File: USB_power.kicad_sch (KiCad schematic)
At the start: 29 parts, among them J14 USB_C_Receptacle_PowerOnly_6P, J16 Conn_01x04, Q3 DMP3013SFV, Q5 DMP3013SFV, U5 CYPD3177-24LQ

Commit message: some changes
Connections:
- net +3.3V is gone; now on net +3.3V_PD: R11.2, R14.2, R16.2, R18.2, R8.2
- net +3.3V_PD: now reaches C52.2, C53.2, C54.2, U5.23 (VDDD)

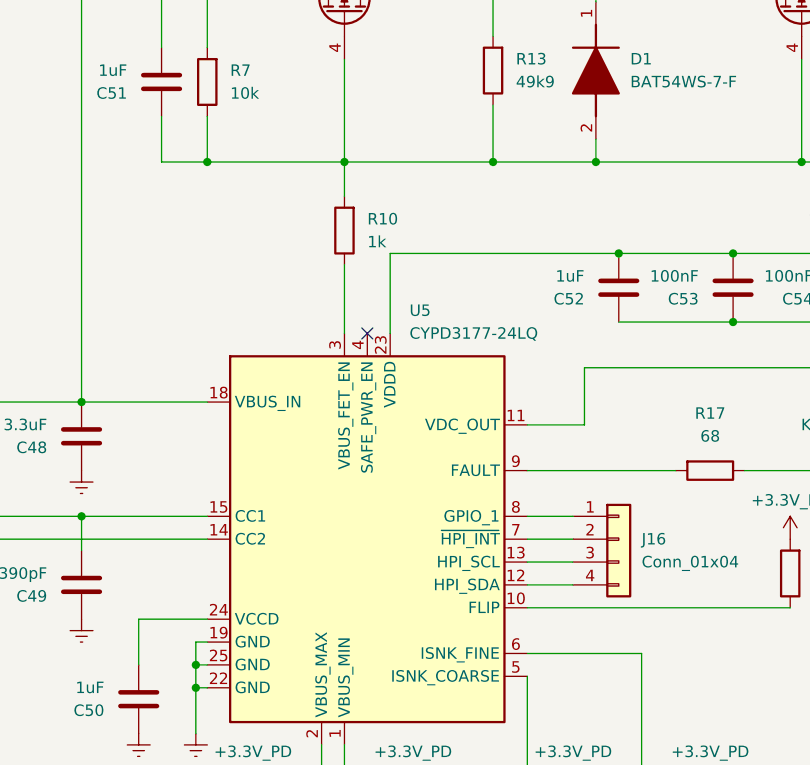
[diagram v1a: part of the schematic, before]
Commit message: experimental thermal pads on bottom side. pins for on/off switch.
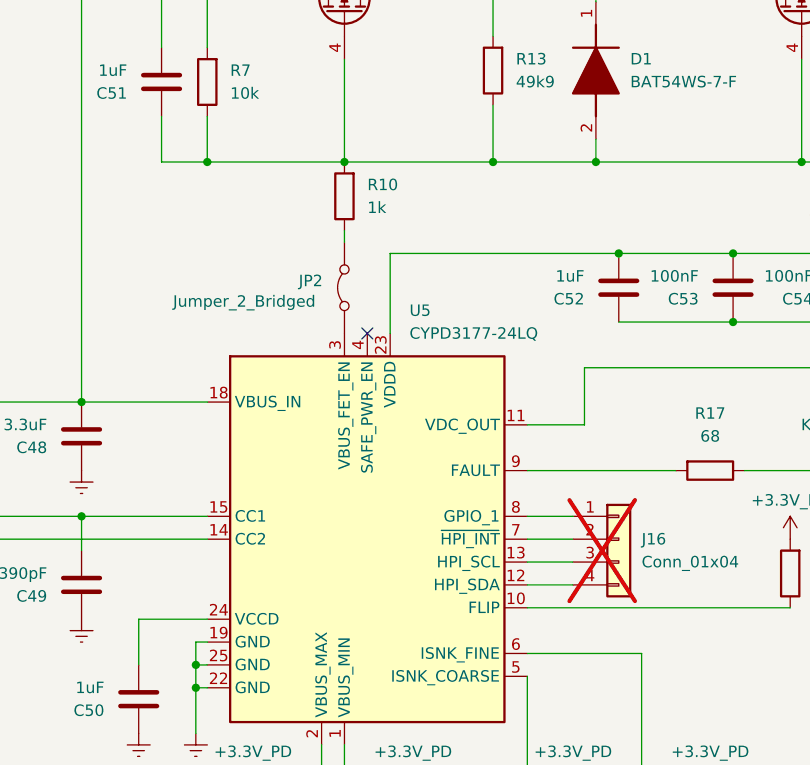
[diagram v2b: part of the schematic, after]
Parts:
- added JP2: Jumper_2_Bridged, Connector_PinHeader_2.54mm:PinHeader_1x02_P2.54mm_Vertical, symbol Jumper:Jumper_2_Bridged
- J16: now not fitted
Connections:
- net at U5.3 (VBUS_FET_EN): now also JP2.1 (A); no longer R10.1
- new net: JP2.2 (B), R10.1
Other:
- moved on the sheet: R10
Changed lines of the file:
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@@
 	(wire
 		(pts
+			(xy 119.38 77.47) (xy 119.38 76.2)
+		)
+		(stroke
+			(width 0)
+			(type default)
+		)
+	)
+	(wire
+		(pts
 			(xy 147.32 68.58) (xy 170.18 68.58)
 		)
@@
 	(wire
 		(pts
-			(xy 119.38 68.58) (xy 119.38 72.39)
-		)
-		(stroke
-			(width 0)
-			(type default)
-		)
-	)
-	(wire
-		(pts
 			(xy 102.87 127) (xy 104.14 127)
 		)
@@
 		)
 	)
-	(wire
-		(pts
-			(xy 119.38 80.01) (xy 119.38 87.63)
-		)
-		(stroke
-			(width 0)
-			(type default)
-		)
-	)
 	(symbol
 		(lib_id "power_ver2:GND")
@@
 	(symbol
 		(lib_id "Device:R")
-		(at 119.38 76.2 180)
+		(at 119.38 72.39 180)
 		(unit 1)
 		(exclude_from_sim no)
@@
 		(fields_autoplaced yes)
 		(property "Reference" "R10"
-			(at 121.92 74.9299 0)
+			(at 121.92 71.1199 0)
 			(effects
 				(font
@@
 		)
 		(property "Value" "1k"
-			(at 121.92 77.4699 0)
+			(at 121.92 73.6599 0)
 			(effects
 				(font
@@
 		)
 		(property "Footprint" "Resistor_SMD:R_0603_1608Metric_Pad0.98x0.95mm_HandSolder"
-			(at 121.158 76.2 90)
+			(at 121.158 72.39 90)
 			(effects
 				(font
@@
 		)
 		(property "Datasheet" "~"
-			(at 119.38 76.2 0)
+			(at 119.38 72.39 0)
 			(effects
 				(font
@@
 		)
 		(property "Description" "Resistor"
-			(at 119.38 76.2 0)
+			(at 119.38 72.39 0)
 			(effects
 				(font
@@
 	)
 	(symbol
+		(lib_id "Jumper:Jumper_2_Bridged")
+		(at 119.38 82.55 90)
+		(unit 1)
+		(exclude_from_sim no)
+		(in_bom yes)
+		(on_board yes)
+		(dnp no)
+		(property "Reference" "JP2"
+			(at 114.3 81.788 90)
+			(effects
+				(font
+					(size 1.27 1.27)
+				)
+				(justify right)
+			)
+		)
+		(property "Value" "Jumper_2_Bridged"
+			(at 100.33 84.074 90)
+			(effects
+				(font
+					(size 1.27 1.27)
+				)
+				(justify right)
+			)
+		)
+		(property "Footprint" "Connector_PinHeader_2.54mm:PinHeader_1x02_P2.54mm_Vertical"
+			(at 119.38 82.55 0)
+			(effects
+				(font
+					(size 1.27 1.27)
+				)
+				(hide yes)
+			)
+		)
+		(property "Datasheet" "~"
+			(at 119.38 82.55 0)
+			(effects
+				(font
+					(size 1.27 1.27)
+				)
+				(hide yes)
+			)
+		)
+		(property "Description" "Jumper, 2-pole, closed/bridged"
+			(at 119.38 82.55 0)
+			(effects
+				(font
+					(size 1.27 1.27)
+				)
+				(hide yes)
+			)
+		)
+		(pin "1"
+		)
+		(pin "2"
+		)
+		(instances
+			(project ""
+				(path "/1f48ed4c-84ce-4e77-88fc-25bf92dcee2d/05204050-0c20-42af-9081-73af52e92f24"
+					(reference "JP2")
+					(unit 1)
+				)
+			)
+		)
+	)
+	(symbol
 		(lib_id "power_ver2:GND")
 		(at 207.01 106.68 0)
@@
 		(in_bom yes)
 		(on_board yes)
-		(dnp no)
+		(dnp yes)
 		(fields_autoplaced yes)
 		(property "Reference" "J16"

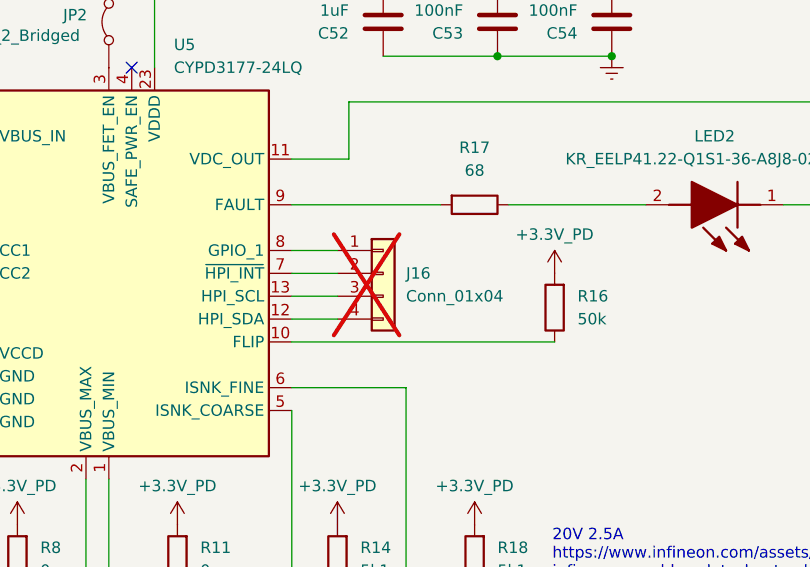
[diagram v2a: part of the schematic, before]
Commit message: bit wider power tracks
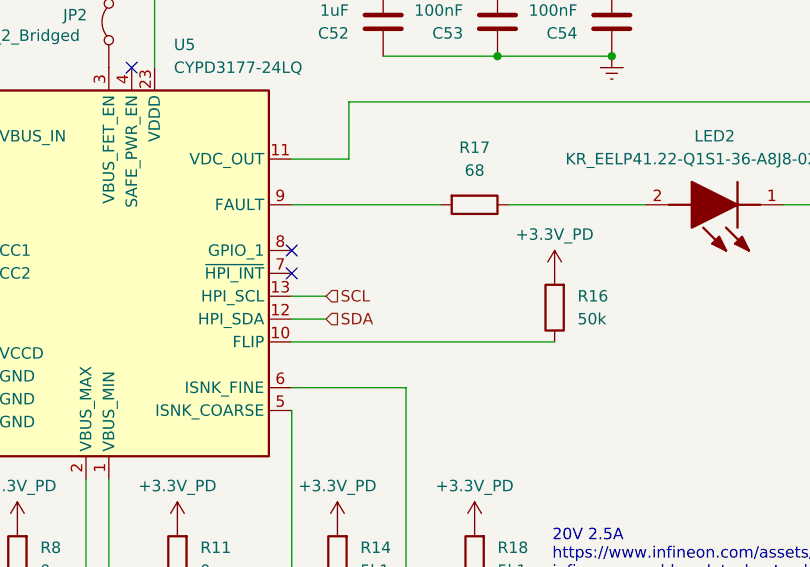
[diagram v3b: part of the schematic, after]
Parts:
- removed J16: Conn_01x04, Connector_PinHeader_2.54mm:PinHeader_1x04_P2.54mm_Vertical, symbol Connector_Generic:Conn_01x04
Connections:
- net SDA: now reaches U5.12 (HPI_SDA)
- net SCL: now reaches U5.13 (HPI_SCL)
- no-connect marks 1 -> 3
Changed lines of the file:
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@@
 	)
 	(no_connect
+		(at 139.7 107.95)
+	)
+	(no_connect
 		(at 121.92 87.63)
 	)
+	(no_connect
+		(at 139.7 110.49)
+	)
 	(wire
 		(pts
@@
 	(wire
 		(pts
+			(xy 143.51 115.57) (xy 139.7 115.57)
+		)
+		(stroke
+			(width 0)
+			(type default)
+		)
+	)
+	(wire
+		(pts
 			(xy 160.02 146.05) (xy 160.02 147.32)
 		)
@@
 	(wire
 		(pts
-			(xy 144.78 107.95) (xy 139.7 107.95)
+			(xy 90.17 95.25) (xy 104.14 95.25)
 		)
 		(stroke
@@
 	(wire
 		(pts
-			(xy 90.17 95.25) (xy 104.14 95.25)
+			(xy 143.51 113.03) (xy 139.7 113.03)
 		)
 		(stroke
@@
 	(wire
 		(pts
-			(xy 144.78 115.57) (xy 139.7 115.57)
-		)
-		(stroke
-			(width 0)
-			(type default)
-		)
-	)
-	(wire
-		(pts
 			(xy 104.14 49.53) (xy 114.3 49.53)
 		)
@@
 	(wire
 		(pts
-			(xy 144.78 113.03) (xy 139.7 113.03)
-		)
-		(stroke
-			(width 0)
-			(type default)
-		)
-	)
-	(wire
-		(pts
 			(xy 102.87 124.46) (xy 102.87 121.92)
 		)
@@
 	(wire
 		(pts
-			(xy 144.78 110.49) (xy 139.7 110.49)
-		)
-		(stroke
-			(width 0)
-			(type default)
-		)
-	)
-	(wire
-		(pts
 			(xy 104.14 63.5) (xy 104.14 68.58)
 		)
@@
 		)
 	)
+	(hierarchical_label "SCL"
+		(shape input)
+		(at 143.51 113.03 0)
+		(effects
+			(font
+				(size 1.27 1.27)
+			)
+			(justify left)
+		)
+	)
+	(hierarchical_label "SDA"
+		(shape input)
+		(at 143.51 115.57 0)
+		(effects
+			(font
+				(size 1.27 1.27)
+			)
+			(justify left)
+		)
+	)
 	(symbol
 		(lib_id "power_ver2:GND")
@@
 					(unit 1)
 				)
-			)
-		)
-	)
-	(symbol
-		(lib_id "Connector_Generic:Conn_01x04")
-		(at 149.86 110.49 0)
-		(unit 1)
-		(exclude_from_sim no)
-		(in_bom yes)
-		(on_board yes)
-		(dnp yes)
-		(fields_autoplaced yes)
-		(property "Reference" "J16"
-			(at 152.4 110.4899 0)
-			(effects
-				(font
-					(size 1.27 1.27)
-				)
-				(justify left)
-			)
-		)
-		(property "Value" "Conn_01x04"
-			(at 152.4 113.0299 0)
-			(effects
-				(font
-					(size 1.27 1.27)
-				)
-				(justify left)
-			)
-		)
-		(property "Footprint" "Connector_PinHeader_2.54mm:PinHeader_1x04_P2.54mm_Vertical"
-			(at 149.86 110.49 0)
-			(effects
-				(font
-					(size 1.27 1.27)
-				)
-				(hide yes)
-			)
-		)
-		(property "Datasheet" "~"
-			(at 149.86 110.49 0)
-			(effects
-				(font
-					(size 1.27 1.27)
-				)
-				(hide yes)
-			)
-		)
-		(property "Description" "Generic connector, single row, 01x04, script generated (kicad-library-utils/schlib/autogen/connector/)"
-			(at 149.86 110.49 0)
-			(effects
-				(font
-					(size 1.27 1.27)
-				)
-				(hide yes)
-			)
-		)
-		(pin "3"
-		)
-		(pin "1"
-		)
-		(pin "2"
-		)
-		(pin "4"
-		)
-		(instances
-			(project "RSC_extension_board"
-				(path "/1f48ed4c-84ce-4e77-88fc-25bf92dcee2d/05204050-0c20-42af-9081-73af52e92f24"
-					(reference "J16")
-					(unit 1)
-				)

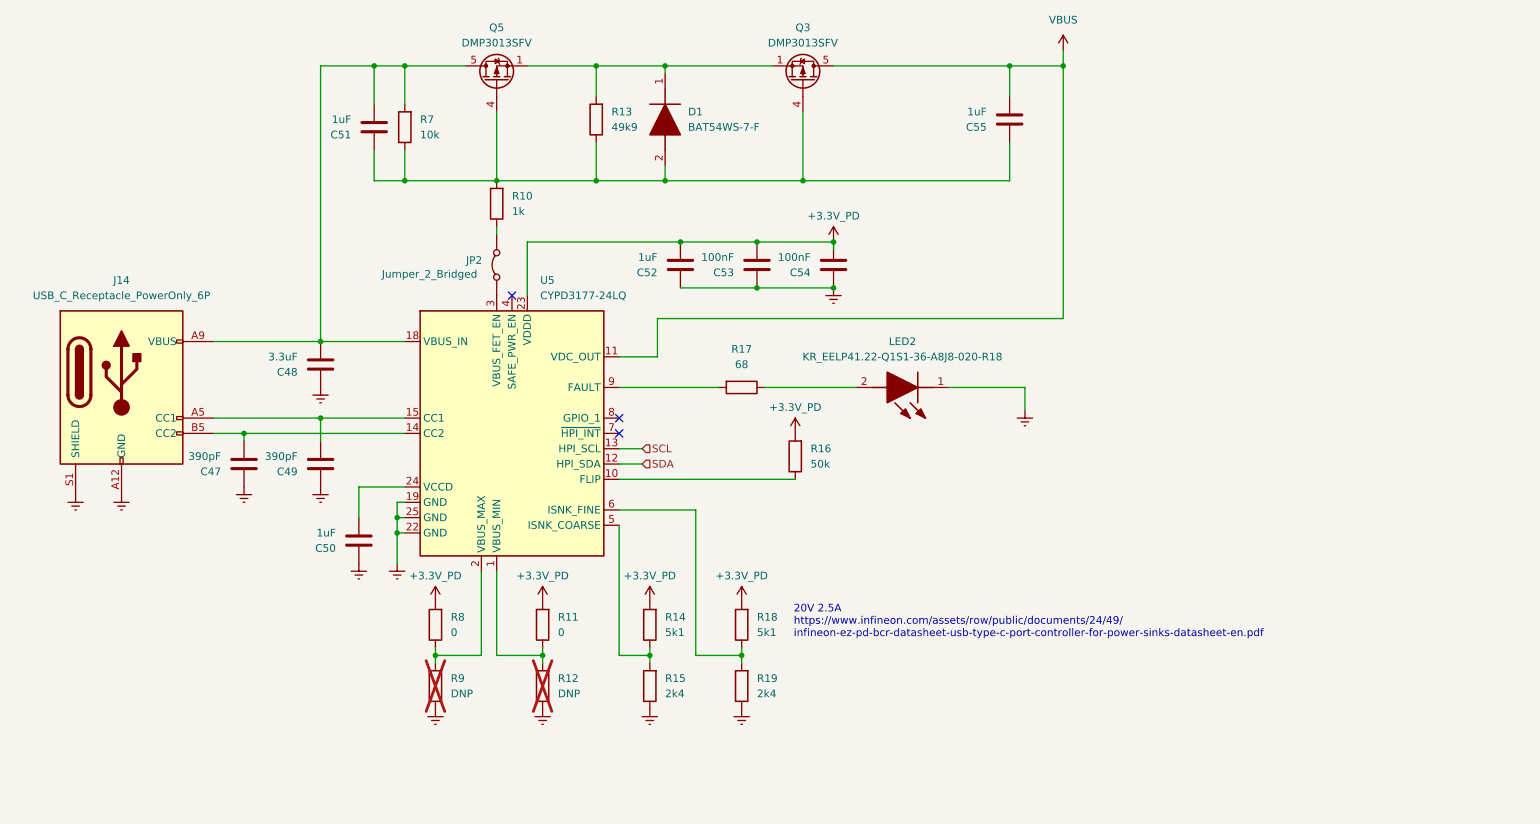
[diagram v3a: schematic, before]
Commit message: pull down resistor on PD mosfet gates- for jumper
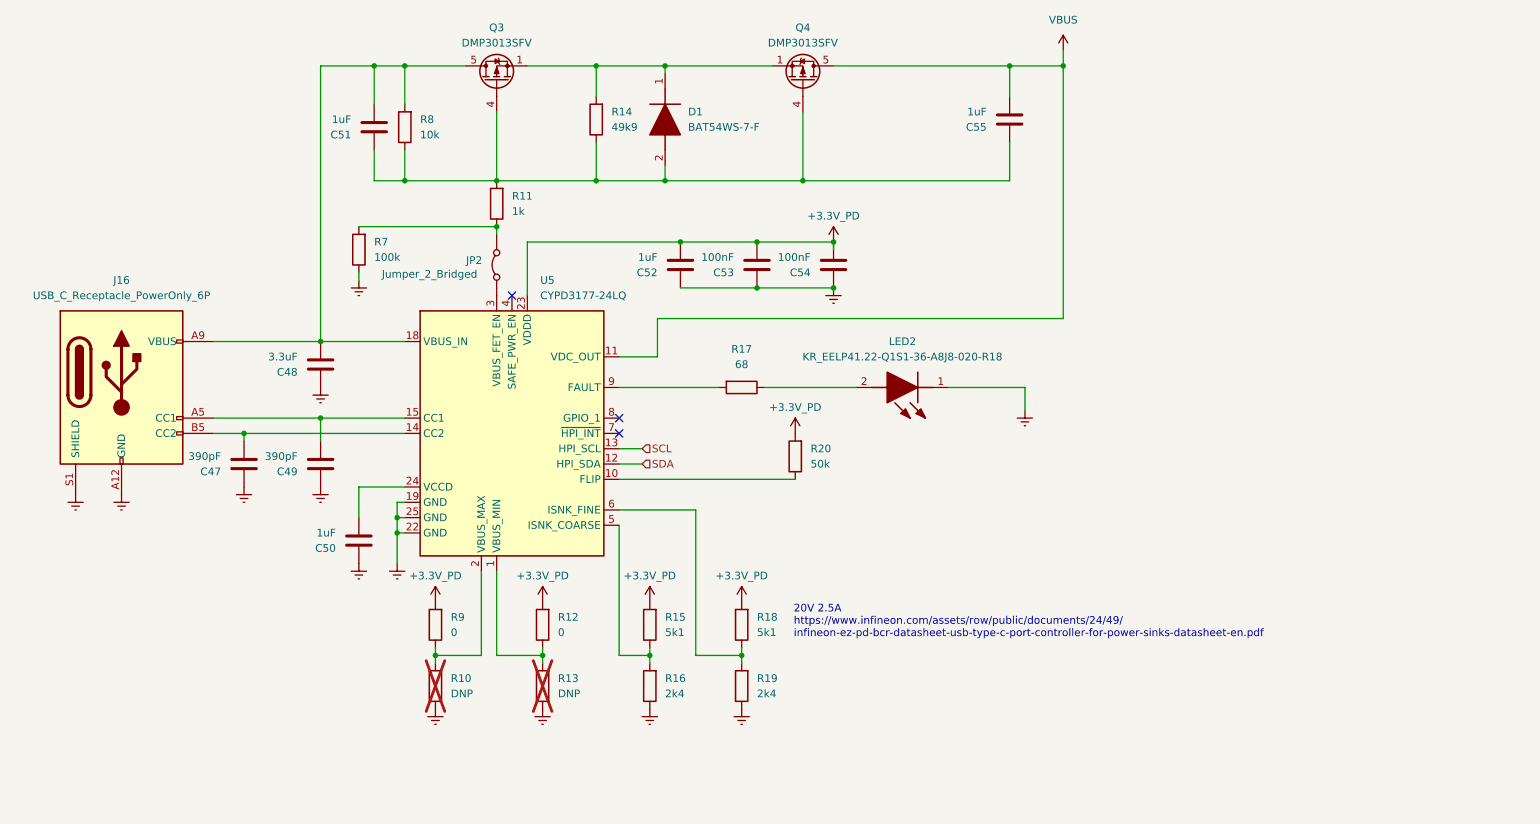
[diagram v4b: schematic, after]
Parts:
- added R7: 100k, Resistor_SMD:R_0603_1608Metric_Pad0.98x0.95mm_HandSolder, symbol Device:R
- renumbered J14 to J16, Q5 to Q3, Q3 to Q4, R9 to R10, R10 to R11, R11 to R12, R12 to R13, R13 to R14, R14 to R15, R15 to R16, R16 to R20, R7 to R8, R8 to R9
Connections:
- net GND: now also R7.1
- net at JP2.2 (B), R11.1: now also R7.2

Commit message: generic 2.54mm headers and testPads excluded from BOM
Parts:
- JP2: now left out of the parts list
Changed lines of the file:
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@@
 		(unit 1)
 		(exclude_from_sim no)
-		(in_bom yes)
+		(in_bom no)
 		(on_board yes)
 		(dnp no)

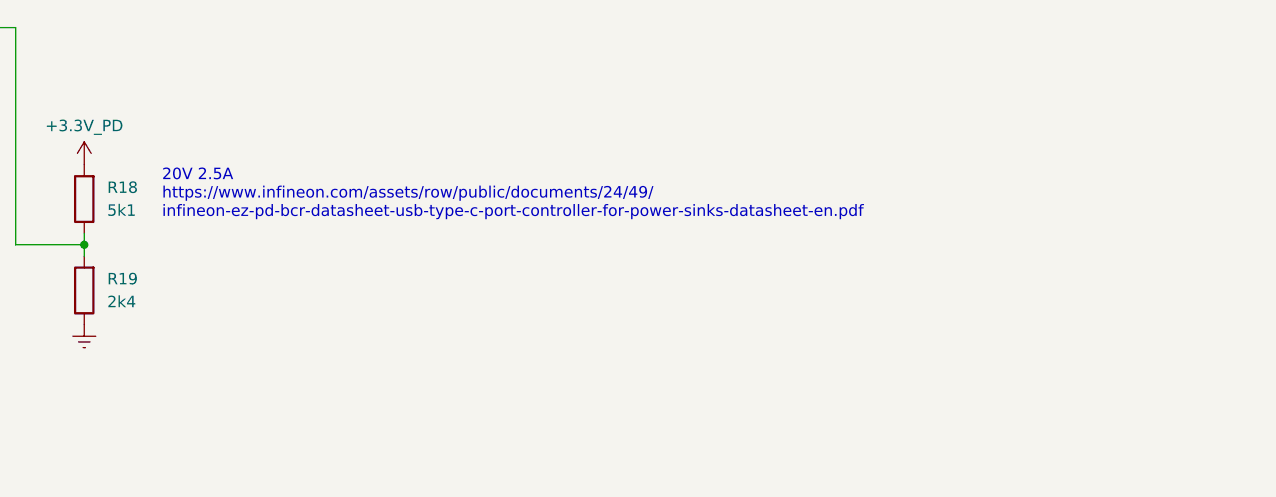
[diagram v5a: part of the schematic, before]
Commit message: added title box information
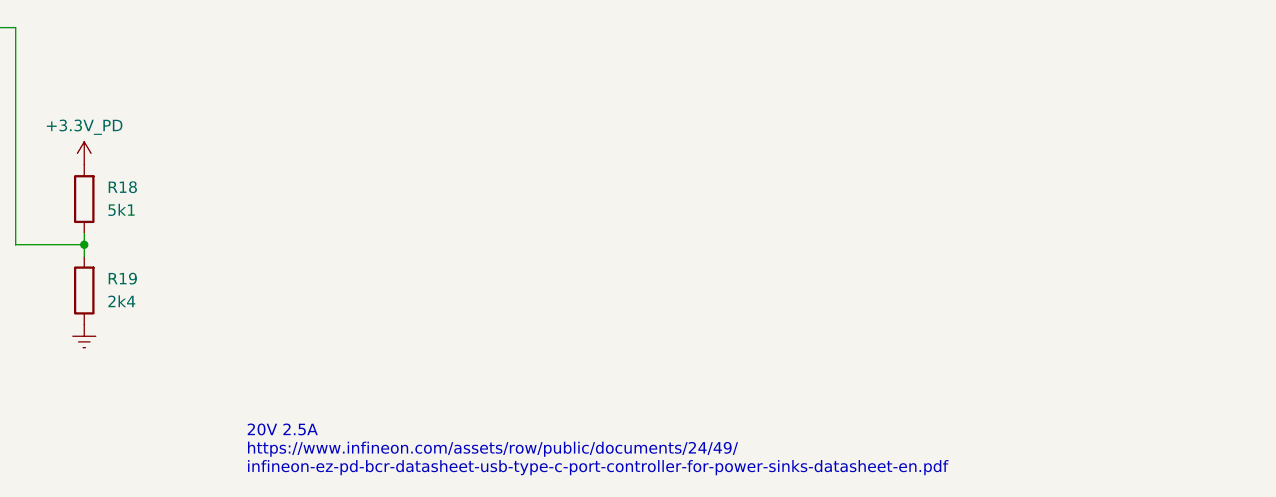
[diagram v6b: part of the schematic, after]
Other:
- title: (none) -> RSC hat board
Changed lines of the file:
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@@
 	(generator_version "9.0")
 	(paper "A4")
+	(title_block
+		(title "RSC hat board")
+		(date "2026-04-30")
+		(rev "A")
+	)
 	(text "20V 2.5A\nhttps://www.infineon.com/assets/row/public/documents/24/49/\ninfineon-ez-pd-bcr-datasheet-usb-type-c-port-controller-for-power-sinks-datasheet-en.pdf"
 		(exclude_from_sim no)
-		(at 168.656 141.732 0)
+		(at 178.054 170.18 0)
 		(effects
 			(font
